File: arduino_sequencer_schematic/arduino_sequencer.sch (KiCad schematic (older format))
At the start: 178 parts, among them J1 AudioJack, J10 AudioJack, J11 AudioJack, J12 AudioJack, J13 AudioJack, J14 AudioJack, J15 AudioJack, J16 Conn_02x05, J17 Conn_01x03, J2 AudioJack, J3 AudioJack, J4 AudioJack, J5 AudioJack, J6 AudioJack, J7 AudioJack, J8 AudioJack, J9 AudioJack, Q1 2N3904, Q10 2N3904, Q11 2N3904, Q2 2N3904, Q3 2N3904, Q4 2N3904, Q5 2N3904, Q6 2N3904, Q7 2N3904, Q8 2N3904, Q9 2N3904, SW1 SW_SPST, SW2 SW_Push, SW3 SW_Push, SW4 SW_Push, SW5 SW_SPST, SW6 SW_SPST, U1 L78L09_TO92, U2 74HC595, U3 TL084, U4 TL084, U5 L7805

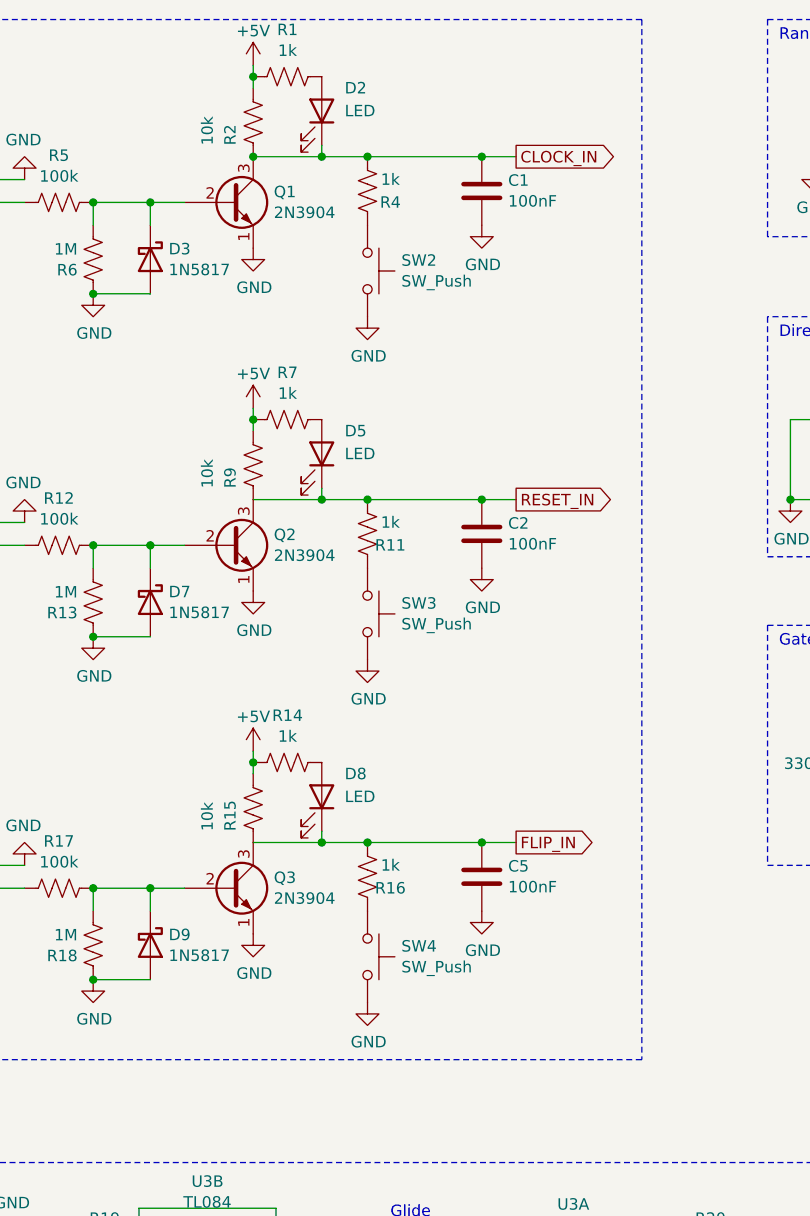
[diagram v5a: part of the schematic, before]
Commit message: Move filter resistor
For improved stability (no faulty triggers)
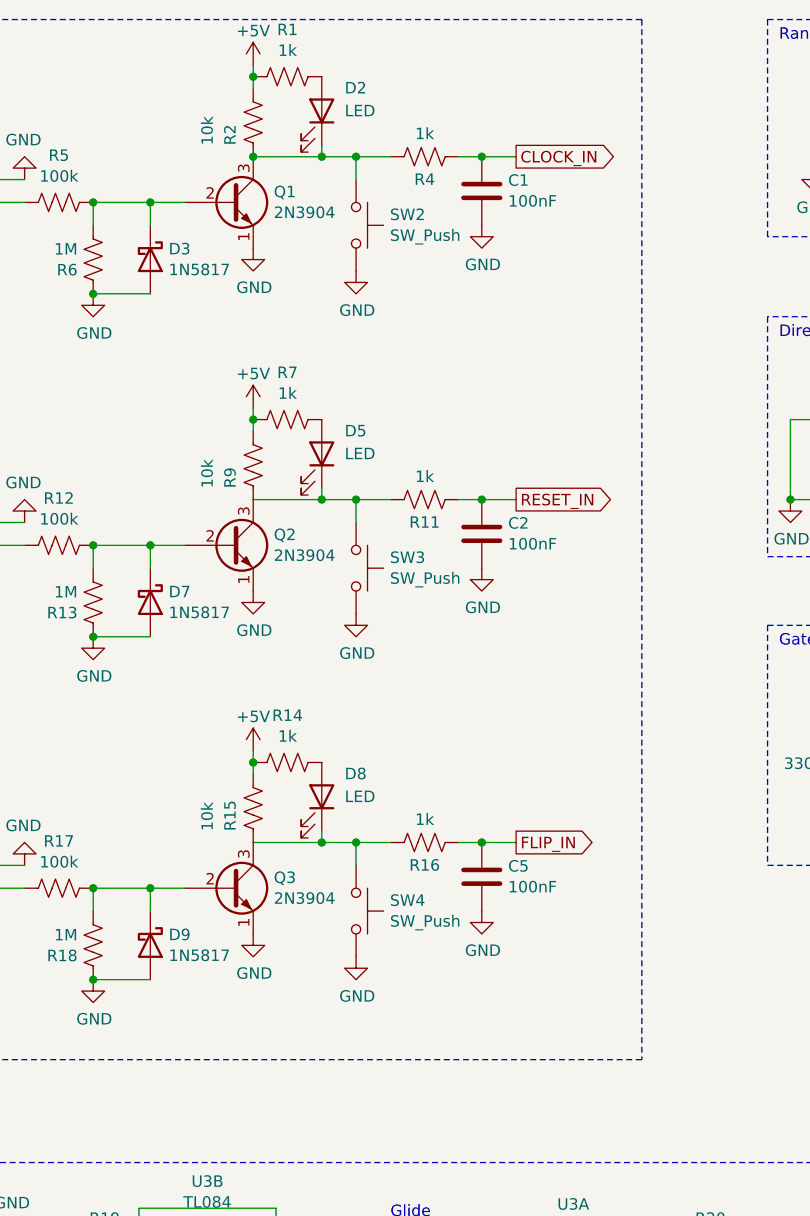
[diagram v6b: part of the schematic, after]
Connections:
- net CLOCK_IN: now also R4.2; no longer D2.1 (K), Q1.3 (C), R2.2, R4.1
- net FLIP_IN: now also R16.2; no longer D8.1 (K), Q3.3 (C), R15.2, R16.1
- net RESET_IN: now also R11.2; no longer D5.1 (K), Q2.3 (C), R11.1, R9.2
- net at SW2.1: now also D2.1 (K), Q1.3 (C), R2.2, R4.1; no longer R4.2
- net at SW3.1: now also D5.1 (K), Q2.3 (C), R11.1, R9.2; no longer R11.2
- net at SW4.1: now also D8.1 (K), Q3.3 (C), R15.2, R16.1; no longer R16.2
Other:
- moved on the sheet: R11, R16, R4, SW2, SW3, SW4
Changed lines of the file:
@@
 L power:GND #PWR010
 U 1 1 5FCE7F1F
-P 3150 2050
-F 0 "#PWR010" H 3150 1800 50  0001 C CNN
-F 1 "GND" H 3155 1877 50  0000 C CNN
-F 2 "" H 3150 2050 50  0001 C CNN
-F 3 "" H 3150 2050 50  0001 C CNN
-	1    3150 2050
+P 3100 1850
+F 0 "#PWR010" H 3100 1600 50  0001 C CNN
+F 1 "GND" H 3105 1677 50  0000 C CNN
+F 2 "" H 3100 1850 50  0001 C CNN
+F 3 "" H 3100 1850 50  0001 C CNN
+	1    3100 1850
 	1    0    0    -1
 $EndComp
@@
 L Device:R_US R4
 U 1 1 5FCDBEC2
-P 3150 1500
-F 0 "R4" H 3250 1450 50  0000 C CNN
-F 1 "1k" H 3250 1550 50  0000 C CNN
-F 2 "TimMJN:R_Axial_DIN0207_L6.3mm_D2.5mm_P10.16mm_Horizontal_Value_SilkS" V 3190 1490 50  0001 C CNN
-F 3 "~" H 3150 1500 50  0001 C CNN
-	1    3150 1500
-	1    0    0    -1
+P 3400 1350
+F 0 "R4" V 3300 1350 50  0000 C CNN
+F 1 "1k" V 3500 1350 50  0000 C CNN
+F 2 "TimMJN:R_Axial_DIN0207_L6.3mm_D2.5mm_P10.16mm_Horizontal_Value_SilkS" V 3440 1340 50  0001 C CNN
+F 3 "~" H 3400 1350 50  0001 C CNN
+	1    3400 1350
+	0    -1   -1   0
 $EndComp
-Connection ~ 3150 1350
-Wire Wire Line
-	3150 1350 3650 1350
 Wire Wire Line
 	2650 2850 2950 2850
@@
 L power:GND #PWR017
 U 1 1 5FD1AC93
-P 3150 3550
-F 0 "#PWR017" H 3150 3300 50  0001 C CNN
-F 1 "GND" H 3155 3377 50  0000 C CNN
-F 2 "" H 3150 3550 50  0001 C CNN
-F 3 "" H 3150 3550 50  0001 C CNN
-	1    3150 3550
+P 3100 3350
+F 0 "#PWR017" H 3100 3100 50  0001 C CNN
+F 1 "GND" H 3105 3177 50  0000 C CNN
+F 2 "" H 3100 3350 50  0001 C CNN
+F 3 "" H 3100 3350 50  0001 C CNN
+	1    3100 3350
 	1    0    0    -1
 $EndComp
@@
 L Device:R_US R11
 U 1 1 5FD1AC99
-P 3150 3000
-F 0 "R11" H 3250 2950 50  0000 C CNN
-F 1 "1k" H 3250 3050 50  0000 C CNN
-F 2 "TimMJN:R_Axial_DIN0207_L6.3mm_D2.5mm_P10.16mm_Horizontal_Value_SilkS" V 3190 2990 50  0001 C CNN
-F 3 "~" H 3150 3000 50  0001 C CNN
-	1    3150 3000
-	1    0    0    -1
+P 3400 2850
+F 0 "R11" V 3300 2850 50  0000 C CNN
+F 1 "1k" V 3500 2850 50  0000 C CNN
+F 2 "TimMJN:R_Axial_DIN0207_L6.3mm_D2.5mm_P10.16mm_Horizontal_Value_SilkS" V 3440 2840 50  0001 C CNN
+F 3 "~" H 3400 2850 50  0001 C CNN
+	1    3400 2850
+	0    -1   -1   0
 $EndComp
 $Comp
 L Switch:SW_Push SW3
 U 1 1 5FD1AC9F
-P 3150 3350
-F 0 "SW3" V 3104 3498 50  0000 L CNN
-F 1 "SW_Push" V 3195 3498 50  0000 L CNN
-F 2 "TimMJN:Mom_push_button_PBS-110" H 3150 3550 50  0001 C CNN
-F 3 "~" H 3150 3550 50  0001 C CNN
-	1    3150 3350
+P 3100 3150
+F 0 "SW3" V 3054 3298 50  0000 L CNN
+F 1 "SW_Push" V 3145 3298 50  0000 L CNN
+F 2 "TimMJN:Mom_push_button_PBS-110" H 3100 3350 50  0001 C CNN
+F 3 "~" H 3100 3350 50  0001 C CNN
+	1    3100 3150
 	0    1    1    0
 $EndComp
@@
 L power:GND #PWR027
 U 1 1 5FD22298
-P 3150 5050
-F 0 "#PWR027" H 3150 4800 50  0001 C CNN
-F 1 "GND" H 3155 4877 50  0000 C CNN
-F 2 "" H 3150 5050 50  0001 C CNN
-F 3 "" H 3150 5050 50  0001 C CNN
-	1    3150 5050
+P 3100 4850
+F 0 "#PWR027" H 3100 4600 50  0001 C CNN
+F 1 "GND" H 3105 4677 50  0000 C CNN
+F 2 "" H 3100 4850 50  0001 C CNN
+F 3 "" H 3100 4850 50  0001 C CNN
+	1    3100 4850
 	1    0    0    -1
 $EndComp
@@
 L Device:R_US R16
 U 1 1 5FD2229E
-P 3150 4500
-F 0 "R16" H 3250 4450 50  0000 C CNN
-F 1 "1k" H 3250 4550 50  0000 C CNN
-F 2 "TimMJN:R_Axial_DIN0207_L6.3mm_D2.5mm_P10.16mm_Horizontal_Value_SilkS" V 3190 4490 50  0001 C CNN
-F 3 "~" H 3150 4500 50  0001 C CNN
-	1    3150 4500
-	1    0    0    -1
+P 3400 4350
+F 0 "R16" V 3300 4350 50  0000 C CNN
+F 1 "1k" V 3500 4350 50  0000 C CNN
+F 2 "TimMJN:R_Axial_DIN0207_L6.3mm_D2.5mm_P10.16mm_Horizontal_Value_SilkS" V 3440 4340 50  0001 C CNN
+F 3 "~" H 3400 4350 50  0001 C CNN
+	1    3400 4350
+	0    -1   -1   0
 $EndComp
 $Comp
 L Switch:SW_Push SW4
 U 1 1 5FD222A4
-P 3150 4850
-F 0 "SW4" V 3104 4998 50  0000 L CNN
-F 1 "SW_Push" V 3195 4998 50  0000 L CNN
-F 2 "TimMJN:Mom_push_button_PBS-110" H 3150 5050 50  0001 C CNN
-F 3 "~" H 3150 5050 50  0001 C CNN
-	1    3150 4850
+P 3100 4650
+F 0 "SW4" V 3054 4798 50  0000 L CNN
+F 1 "SW_Push" V 3145 4798 50  0000 L CNN
+F 2 "TimMJN:Mom_push_button_PBS-110" H 3100 4850 50  0001 C CNN
+F 3 "~" H 3100 4850 50  0001 C CNN
+	1    3100 4650
 	0    1    1    0
 $EndComp
@@
 	1    0    0    -1
 $EndComp
-Connection ~ 3650 2850
 Wire Wire Line
 	3650 2850 3800 2850
@@
 Wire Wire Line
 	11450 3650 11450 3750
-Connection ~ 3150 2850
-Wire Wire Line
-	3150 2850 3650 2850
-Connection ~ 3150 4350
-Wire Wire Line
-	3150 4350 3650 4350
-Connection ~ 3650 1350
 Wire Wire Line
 	3650 1350 3800 1350
-Connection ~ 3650 4350
 Wire Wire Line
 	3650 4350 3800 4350
@@
 L Switch:SW_Push SW2
 U 1 1 5FCE0085
-P 3150 1850
-F 0 "SW2" V 3104 1998 50  0000 L CNN
-F 1 "SW_Push" V 3195 1998 50  0000 L CNN
-F 2 "TimMJN:Mom_push_button_PBS-110" H 3150 2050 50  0001 C CNN
-F 3 "~" H 3150 2050 50  0001 C CNN
-	1    3150 1850
+P 3100 1650
+F 0 "SW2" V 3054 1798 50  0000 L CNN
+F 1 "SW_Push" V 3145 1798 50  0000 L CNN
+F 2 "TimMJN:Mom_push_button_PBS-110" H 3100 1850 50  0001 C CNN
+F 3 "~" H 3100 1850 50  0001 C CNN
+	1    3100 1650
 	0    1    1    0
 $EndComp
@@
 Wire Wire Line
 	2950 1300 2950 1350
-Connection ~ 2950 1350
-Wire Wire Line
-	2950 1350 3150 1350
 $Comp
 L Device:R_US R9
@@
 Connection ~ 2950 2850
 Wire Wire Line
-	2950 2850 3150 2850
+	2950 2850 3100 2850
 Wire Wire Line
 	2950 4300 2950 4350
 Connection ~ 2950 4350
 Wire Wire Line
-	2950 4350 3150 4350
+	2950 4350 3100 4350
 Text GLabel 8500 2000 3    50   Output ~ 0
 DEC_LED
@@
 Text Notes 10350 1900 0    50   ~ 0
 Expansion header
+Wire Wire Line
+	3550 1350 3650 1350
+Connection ~ 3650 1350
+Wire Wire Line
+	3550 4350 3650 4350
+Connection ~ 3650 4350
+Wire Wire Line
+	3550 2850 3650 2850
+Connection ~ 3650 2850
+Wire Wire Line
+	3100 4450 3100 4350
+Connection ~ 3100 4350
+Wire Wire Line
+	3100 4350 3250 4350
+Wire Wire Line
+	3100 2950 3100 2850
+Connection ~ 3100 2850
+Wire Wire Line
+	3100 2850 3250 2850
+Wire Wire Line
+	3100 1450 3100 1350
+Wire Wire Line
+	3100 1350 3250 1350
+Wire Wire Line
+	3100 1350 2950 1350
+Connection ~ 3100 1350
+Connection ~ 2950 1350
 $EndSCHEMATC

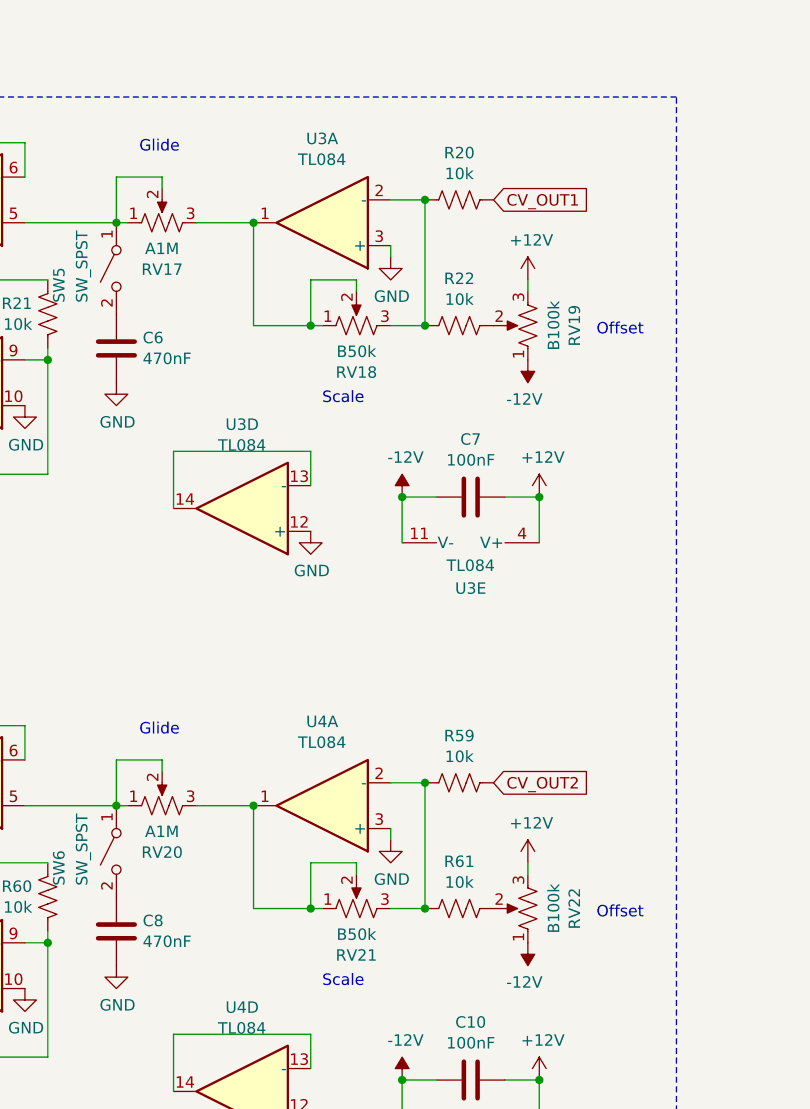
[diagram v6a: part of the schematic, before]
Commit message: Finetuned gain/offset ranges
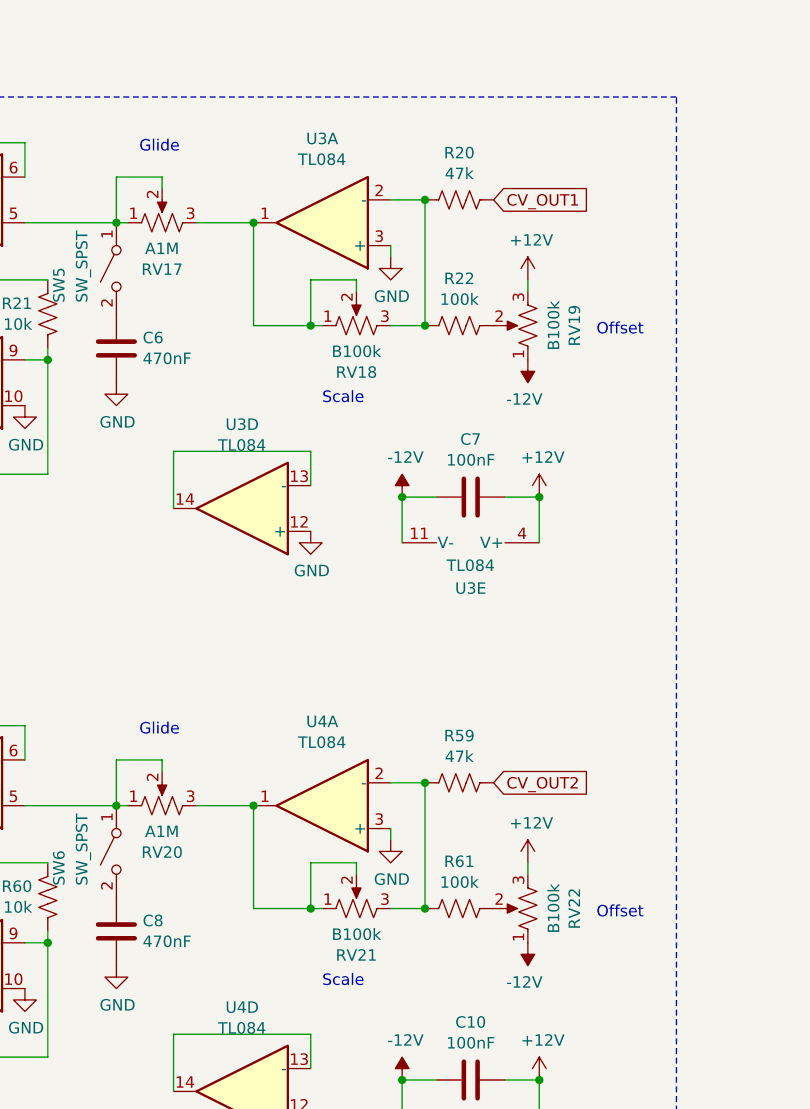
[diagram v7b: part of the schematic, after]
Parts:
- R20, R59: value 10k -> 47k
- R22, R61: value 10k -> 100k
- RV18, RV21: value B50k -> B100k
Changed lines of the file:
@@
 P 4650 8750
 F 0 "R59" V 4445 8750 50  0000 C CNN
-F 1 "10k" V 4536 8750 50  0000 C CNN
+F 1 "47k" V 4536 8750 50  0000 C CNN
 F 2 "TimMJN:R_Axial_DIN0207_L6.3mm_D2.5mm_P10.16mm_Horizontal_Value_SilkS" V 4690 8740 50  0001 C CNN
 F 3 "~" H 4650 8750 50  0001 C CNN
@@
 P 4650 9300
 F 0 "R61" V 4445 9300 50  0000 C CNN
-F 1 "10k" V 4536 9300 50  0000 C CNN
+F 1 "100k" V 4536 9300 50  0000 C CNN
 F 2 "TimMJN:R_Axial_DIN0207_L6.3mm_D2.5mm_P10.16mm_Horizontal_Value_SilkS" V 4690 9290 50  0001 C CNN
 F 3 "~" H 4650 9300 50  0001 C CNN
@@
 P 4200 9300
 F 0 "RV21" V 3995 9300 50  0000 C CNN
-F 1 "B50k" V 4086 9300 50  0000 C CNN
+F 1 "B100k" V 4086 9300 50  0000 C CNN
 F 2 "Potentiometer_THT:Potentiometer_Alpha_RD901F-40-00D_Single_Vertical" H 4200 9300 50  0001 C CNN
 F 3 "~" H 4200 9300 50  0001 C CNN
@@
 P 4650 6200
 F 0 "R20" V 4445 6200 50  0000 C CNN
-F 1 "10k" V 4536 6200 50  0000 C CNN
+F 1 "47k" V 4536 6200 50  0000 C CNN
 F 2 "TimMJN:R_Axial_DIN0207_L6.3mm_D2.5mm_P10.16mm_Horizontal_Value_SilkS" V 4690 6190 50  0001 C CNN
 F 3 "~" H 4650 6200 50  0001 C CNN
@@
 P 4650 6750
 F 0 "R22" V 4445 6750 50  0000 C CNN
-F 1 "10k" V 4536 6750 50  0000 C CNN
+F 1 "100k" V 4536 6750 50  0000 C CNN
 F 2 "TimMJN:R_Axial_DIN0207_L6.3mm_D2.5mm_P10.16mm_Horizontal_Value_SilkS" V 4690 6740 50  0001 C CNN
 F 3 "~" H 4650 6750 50  0001 C CNN
@@
 P 4200 6750
 F 0 "RV18" V 3995 6750 50  0000 C CNN
-F 1 "B50k" V 4086 6750 50  0000 C CNN
+F 1 "B100k" V 4086 6750 50  0000 C CNN
 F 2 "Potentiometer_THT:Potentiometer_Alpha_RD901F-40-00D_Single_Vertical" H 4200 6750 50  0001 C CNN
 F 3 "~" H 4200 6750 50  0001 C CNN
